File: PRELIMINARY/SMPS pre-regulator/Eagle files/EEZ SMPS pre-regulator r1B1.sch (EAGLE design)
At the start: 107 parts, among them IC1 LTC3864, IC2 Si8610BC-B-IS, IC3 MC79L05, IC4 MC78L05, IC5 LM5574, IC6 LP2951SO8, IC7 TLC555, Q1 SUD19P06-60, Q2 MMBT5401, Q3 2N7002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

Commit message: Few PCB layout correction for SMPS pre-regulator r1B1
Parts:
- R1: device rcl:R-EU_R0805 -> rcl:R-EU_R1206
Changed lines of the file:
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@@
 <part name="FRAME7" library="frames" deviceset="DINA4_L" device=""/>
 <part name="C25" library="rcl" deviceset="C-EU" device="C0805" value="330n"/>
-<part name="R1" library="rcl" deviceset="R-EU_" device="R0805" value="18K"/>
+<part name="R1" library="rcl" deviceset="R-EU_" device="R1206" value="18K"/>
 <part name="R21" library="rcl" deviceset="R-EU_" device="R0805" value="390R"/>
 <part name="LED1" library="led" deviceset="LED" device="CHIPLED_0805" value="HSMY-C170"/>

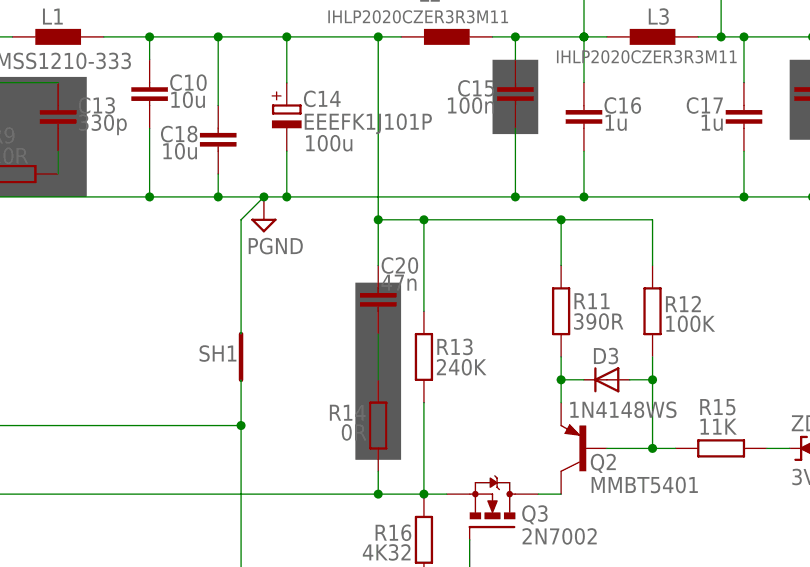
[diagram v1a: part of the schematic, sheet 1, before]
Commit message: SMPS pre-regulator small corrections
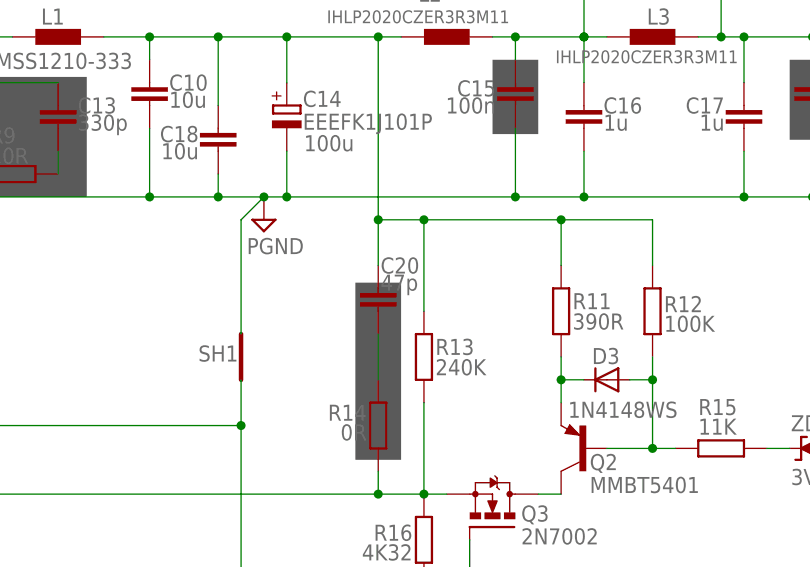
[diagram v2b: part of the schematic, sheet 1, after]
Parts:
- C20: value 47n -> 47p
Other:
- note added: "Note 1.1: Q1 and D2 requires thermal bridge/heatsink. See layer 90 in Board editor for an example."
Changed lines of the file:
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@@
 <layer number="101" name="Pinouts" color="13" fill="1" visible="yes" active="yes"/>
 <layer number="102" name="Signals" color="3" fill="1" visible="yes" active="yes"/>
-<layer number="103" name="extrainfo" color="6" fill="0" visible="yes" active="yes"/>
-<layer number="104" name="comments" color="9" fill="1" visible="no" active="yes"/>
+<layer number="103" name="extrainfo" color="5" fill="0" visible="yes" active="yes"/>
+<layer number="104" name="comments" color="9" fill="1" visible="yes" active="yes"/>
 <layer number="105" name="tPlate" color="7" fill="1" visible="yes" active="yes"/>
 <layer number="106" name="bPlate" color="7" fill="1" visible="yes" active="yes"/>
 <layer number="107" name="Crop" color="7" fill="1" visible="yes" active="yes"/>
-<layer number="108" name="Notes" color="5" fill="1" visible="yes" active="yes"/>
 <layer number="109" name="fp9" color="7" fill="1" visible="no" active="no"/>
 <layer number="110" name="110" color="7" fill="1" visible="no" active="no"/>
@@
 <layer number="132" name="bAdjust" color="7" fill="1" visible="no" active="no"/>
 <layer number="144" name="Drill_legend" color="7" fill="1" visible="no" active="no"/>
+<layer number="150" name="Notes" color="7" fill="1" visible="no" active="no"/>
 <layer number="151" name="HeatSink" color="14" fill="1" visible="no" active="no"/>
 <layer number="152" name="_bDocu" color="7" fill="1" visible="no" active="no"/>
@@
 <layer number="223" name="223bmp" color="24" fill="1" visible="no" active="no"/>
 <layer number="224" name="224bmp" color="25" fill="1" visible="no" active="no"/>
-<layer number="225" name="225bmp" color="26" fill="1" visible="no" active="yes"/>
-<layer number="226" name="226bmp" color="27" fill="1" visible="no" active="yes"/>
-<layer number="227" name="227bmp" color="28" fill="1" visible="no" active="yes"/>
-<layer number="228" name="228bmp" color="29" fill="1" visible="no" active="yes"/>
 <layer number="231" name="Eagle3D_PG1" color="7" fill="1" visible="no" active="no"/>
 <layer number="232" name="Eagle3D_PG2" color="7" fill="1" visible="no" active="no"/>
@@
 <part name="FRAME3" library="frames" deviceset="DINA4_L" device=""/>
 <part name="R14" library="rcl" deviceset="R-EU_" device="R0805" value="0R"/>
-<part name="C20" library="rcl" deviceset="C-EU" device="C0805" value="47n"/>
+<part name="C20" library="rcl" deviceset="C-EU" device="C0805" value="47p"/>
 <part name="R13" library="rcl" deviceset="R-EU_" device="R0805" value="240K"/>
 <part name="R16" library="rcl" deviceset="R-EU_" device="R0805" value="4K32"/>
@@
 <rectangle x1="111.125" y1="128.905" x2="118.11" y2="132.715" layer="97"/>
 <rectangle x1="182.88" y1="62.23" x2="187.96" y2="81.915" layer="97"/>
-<text x="50.165" y="119.38" size="1.778" layer="108">Fsw=350kHz (when grounded)</text>
-<text x="144.145" y="122.555" size="1.778" layer="108">Ilimit=4.06A (95mV/20mOhm-1.04/2)</text>
-<text x="144.145" y="125.095" size="1.778" layer="108">Rsense=20mOhm (95mV/(1.3*(3A+1.04/2)))</text>
-<text x="144.145" y="127.635" size="1.778" layer="108">Ilripple=1.04A for Vout=20V, L=33uH, Vin=50V (((20V/350kHz*33uH)(1-20V/50V)))</text>
-<text x="63.5" y="130.175" size="1.778" layer="108">tss=8ms</text>
+<text x="50.165" y="119.38" size="1.778" layer="103">Fsw=350kHz (when grounded)</text>
+<text x="144.145" y="122.555" size="1.778" layer="103">Ilimit=4.06A (95mV/20mOhm-1.04/2)</text>
+<text x="144.145" y="125.095" size="1.778" layer="103">Rsense=20mOhm (95mV/(1.3*(3A+1.04/2)))</text>
+<text x="144.145" y="127.635" size="1.778" layer="103">Ilripple=1.04A for Vout=20V, L=33uH, Vin=50V (((20V/350kHz*33uH)(1-20V/50V)))</text>
+<text x="63.5" y="130.175" size="1.778" layer="103">tss=8ms</text>
 <text x="2.54" y="7.62" size="1.778" layer="94">Licensed under the TAPR Open Hardware License (www.tapr.org/OHL)</text>
 <text x="2.54" y="2.54" size="1.778" layer="94">Repository: https://github.com/eez-open</text>
@@
 <circle x="69.85" y="24.13" radius="0.635" width="0.1524" layer="101"/>
 <text x="71.755" y="24.765" size="1.4224" layer="101" rot="MR180">3 Gnd</text>
-<text x="84.455" y="66.675" size="1.778" layer="108">Sync In</text>
-<text x="6.985" y="66.04" size="1.778" layer="108">Sync Out</text>
+<text x="84.455" y="66.675" size="1.778" layer="103">Sync In</text>
+<text x="6.985" y="66.04" size="1.778" layer="103">Sync Out</text>
 <rectangle x1="129.54" y1="147.955" x2="134.62" y2="154.305" layer="97"/>
+<text x="5.08" y="13.335" size="1.778" layer="103">Note 1.1: Q1 and D2 requires thermal bridge/heatsink. See layer 90 in Board editor for an example. </text>
 </plain>
 <instances>
@@
 <rectangle x1="95.885" y1="114.3" x2="107.315" y2="127.635" layer="97"/>
 <text x="22.86" y="131.445" size="1.27" layer="96">(LQH32PN2R2NN0L)</text>
-<text x="211.455" y="153.67" size="1.27" layer="108" rot="MR180">-5V</text>
-<text x="206.375" y="133.35" size="1.27" layer="108">+5V</text>
-<text x="147.955" y="133.35" size="1.27" layer="108">+9V</text>
+<text x="211.455" y="153.67" size="1.27" layer="103" rot="MR180">-5V</text>
+<text x="206.375" y="133.35" size="1.27" layer="103">+5V</text>
+<text x="147.955" y="133.35" size="1.27" layer="103">+9V</text>
 <text x="165.1" y="26.035" size="2.54" layer="94" font="vector">Bias power supply with SMPS pre-regulator</text>
-<text x="114.935" y="100.33" size="1.27" layer="108">+1.225V</text>
+<text x="114.935" y="100.33" size="1.27" layer="103">+1.225V</text>
 <text x="157.48" y="113.665" size="1.778" layer="96">Yellow</text>
-<text x="135.255" y="156.21" size="1.27" layer="108">-9V</text>
+<text x="135.255" y="156.21" size="1.27" layer="103">-9V</text>
 <text x="2.54" y="7.62" size="1.778" layer="94">Licensed under the TAPR Open Hardware License (www.tapr.org/OHL)</text>
 <text x="2.54" y="2.54" size="1.778" layer="94">Repository: https://github.com/eez-open</text>
 <text x="2.54" y="5.08" size="1.778" layer="94">More info at http://www.envox.hr/eez</text>
-<text x="230.505" y="97.155" size="1.27" layer="108">Tant.</text>
+<text x="230.505" y="97.155" size="1.27" layer="103">Tant.</text>
 <text x="118.11" y="38.1" size="1.27" layer="96">e.g. Farnell: 1187100</text>
 <text x="118.11" y="40.005" size="1.778" layer="96">10K NTC</text>
 <text x="118.11" y="36.195" size="1.27" layer="96">or TME: NTC-K45-10</text>
-<text x="86.995" y="57.785" size="1.27" layer="108">Fout: ~100Hz/oC (NTC sensor 10K, beta: 4300K) for range 25-70oC</text>
+<text x="86.995" y="57.785" size="1.27" layer="103">Fout: ~100Hz/oC (NTC sensor 10K, beta: 4300K) for range 25-70oC</text>
 <text x="7.62" y="66.04" size="1.778" layer="97" rot="MR180">V/F converter for temperature sensor (optional)</text>
-<text x="104.14" y="45.085" size="1.778" layer="108">TEMP</text>
+<text x="104.14" y="45.085" size="1.778" layer="103">TEMP</text>
 <wire x1="2.54" y1="68.58" x2="261.62" y2="68.58" width="0.1524" layer="97" style="shortdash"/>
 </plain>
